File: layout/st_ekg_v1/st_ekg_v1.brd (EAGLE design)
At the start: 59.4 x 56.8 mm, 31 parts, among them J1 SJ1-3523N

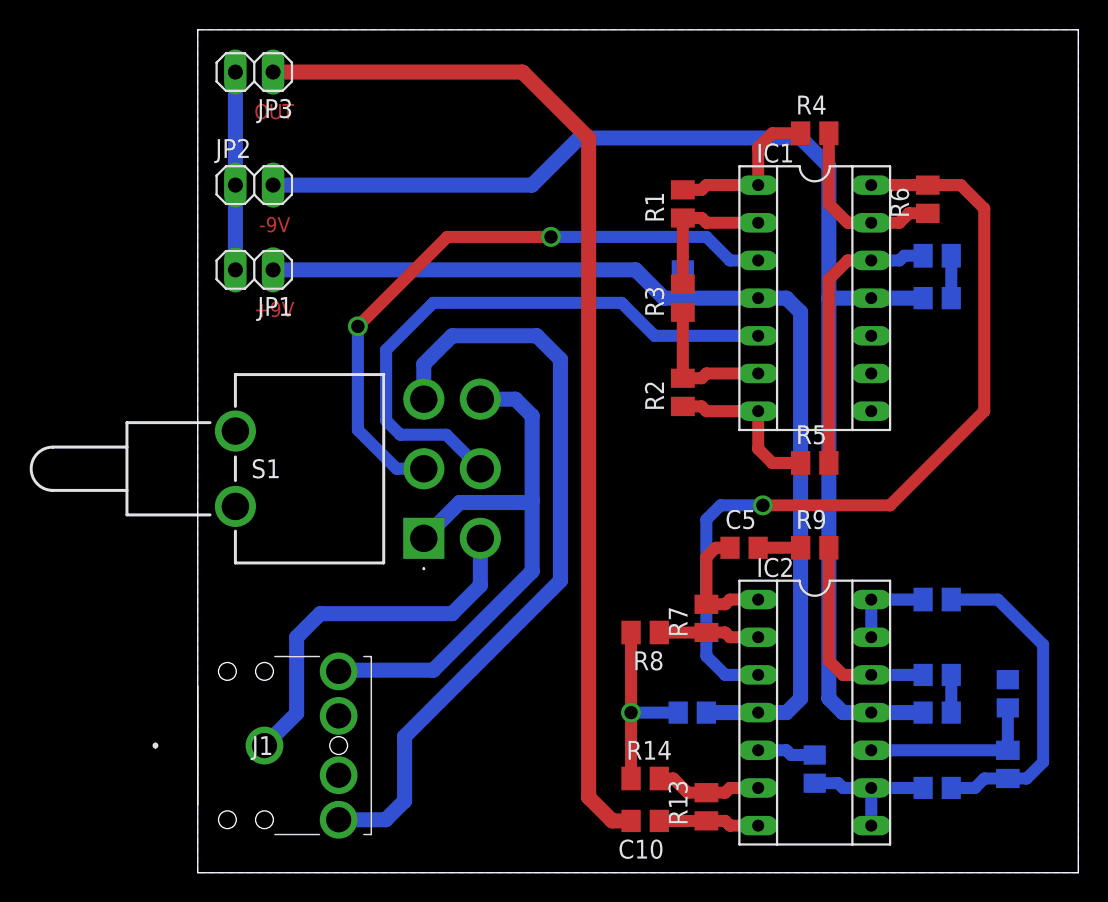
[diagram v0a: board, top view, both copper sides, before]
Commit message: Modify layout to include only bottom paths on pin headers
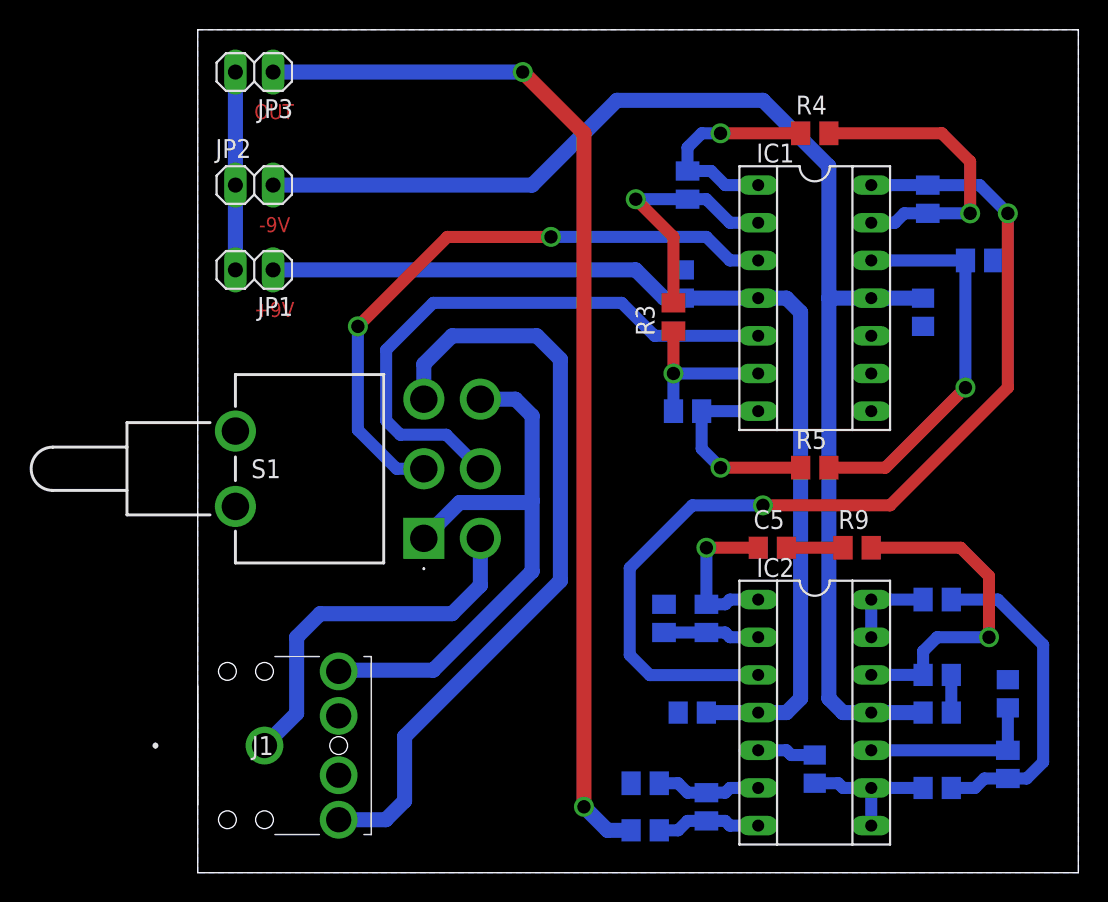
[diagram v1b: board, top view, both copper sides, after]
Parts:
- moved R11 2.88 mm to (52.7, 41.3)
- moved R9 2.86 mm to (44.5, 21.9)
- moved C5 1.91 mm to (38.7, 21.9)
- moved R8 1.59 mm to (31.4, 17.1), flipped to the bottom, turned to 90 degrees
- moved R3 1.42 mm to (32.1, 37.5)
- moved C2 1.35 mm to (48.9, 37.8), turned to 270 degrees
- moved R2 1.31 mm to (33.0, 31.1), flipped to the bottom, turned to 0 degrees
- moved R1 1.31 mm to (33.0, 46.4), flipped to the bottom
- moved C10 0.64 mm to (30.2, 2.86), flipped to the bottom, turned to 0 degrees
- moved R14 0.32 mm to (30.2, 6.03), flipped to the bottom, turned to 180 degrees
- moved R5 0.32 mm to (41.6, 27.3)
- flipped R13 to the bottom
- flipped R6 to the bottom
- flipped R7 to the bottom
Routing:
- net GND: track 31.8 -> 15.9 mm, vias 1 -> 0
- net N$10: track 56.9 -> 67.4 mm, vias 1 -> 2
- net N$5: track 12.2 -> 20.7 mm, vias 0 -> 1
- net N$15: track 14.4 -> 22.8 mm, vias 0 -> 1
- net N$4: track 9.66 -> 17.0 mm, vias 0 -> 1
- net N$7: track 19.4 -> 26.4 mm, vias 0 -> 1
- net N$8: track 11.0 -> 14.8 mm, vias 0 -> 1
- net N$9: track 11.0 -> 13.5 mm, vias 0 -> 1
- net N$13: track 8.66 -> 10.9 mm, vias 0 -> 1
- net V-: track 88.5 -> 90.6 mm
- net N$6: track 9.66 -> 11.1 mm, vias 0 -> 1
- net N$14: track 2.86 -> 3.81 mm
- net OUT: track 71.1 -> 71.9 mm, vias 0 -> 2
